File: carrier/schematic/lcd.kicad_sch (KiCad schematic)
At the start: 17 parts, among them J12001 AFC07-S40FCA-00, U12001 SY7201ABC

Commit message: board: four board-management HW blocks on a manually-gated +3V3_AUX (BOARDHW)
The four services the carrier was missing — all behind ONE manual power enable
(C1) on two new sheets split so neither defeats the placer's rail-stub router:

  board_aux       — the gate + I2C isolator (infrastructure)
  board_services  — ID-EEPROM + RTC + watchdog + QWIIC (the peripherals)

WHAT LANDED
  * 24AA025E48 (C129895)  ID-EEPROM with a factory EUI-48 **MAC** for the
      LAN8720/RJ45 — strapped 0x51 (0x50 is the FMC EEPROM).
  * RV-3028-C7 (C3019759) I2C RTC, integrated DTCXO (no crystal), CR1220 coin
      cell (KH-CR1220-2) with auto-switchover, 0x52.
  * TPS3823-33 (C7719)    supervisor + windowed watchdog.
  * ZX-SH1.0-4PWT (C7430446)  QWIIC / STEMMA-QT expansion (gated 3V3 + the
      isolated AUX I2C).
  * SY6280 gate + DSHP04 DIP + PCA9306 isolator complete the infrastructure.

CONSTRAINTS (the user's three standing requirements)
  C1 manual enable "like the previous": +3V3_AUX is a SY6280 load switch whose
     EN is a default-OFF DSHP04 DIP (100k pulldown) — the same gated-module
     idiom, self-contained so it touches none of the dense rail/EN sheets.
  C2 "no watchdog reset during power-up": THREE independent guards — (1) the
     supervisor's VDD is the default-OFF +3V3_AUX, so it is UNPOWERED through
     power-up; (2) the TPS3823 disables its watchdog while WDI floats, and WDI
     is driven only by the PL (WATCHDOG_KICK, Hi-Z until the fabric is up); (3)
     RESET# is a firmware-mediated PL EVENT (J3.31), never a rail/POR line.
  C3 Zynq-agnostic: the only SoM-side signals (the 2 watchdog lines) ride PL
     bank-35 IO by their contract net names (IO_L16_N/P_35 -> J3.29/31); xdc.py
     emits the constraints live — nothing hard-codes the Zynq part.

LAW 0 (electrical integrity): the peripherals sit on the GATED rail but their
bus is the always-on STM32_I2C2 management bus. A PCA9306 bridges them with EN
tied to +3V3_AUX, so the switch OPENS whenever the rail is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
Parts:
- renumbered C12001 to C14001, C12002 to C14002, C12003 to C14003, D12001 to D14001, J12001 to J14001, L12001 to L14001, R12001 to R14001, R12002 to R14002, R12003 to R14003, R12004 to R14004, R12005 to R14005, R12006 to R14006, R12007 to R14007, TP12001 to TP14001, TP12002 to TP14002, TP12003 to TP14003, U12001 to U14001

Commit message: audit fixes: QWIIC ESD on its own sheet + firmware I2C-map completeness
Acting on a multi-agent adversarial re-audit of the 28-sheet board. Each
finding was independently re-verified before action — two confident "HIGH"
findings were FALSE POSITIVES whose proposed fixes would have INTRODUCED bugs,
and are documented-rejected, not applied:

  * "DSHP04 switches in parallel" — wrong. The footprint pads prove the pairing
    by physical opposition (switch n = pads n & 9-n): switch 1 = pads 1&8 is the
    only one on EN_AUX; the other even pins (2/4/6) are NC, identical to the
    proven bringup_rails SW6 idiom. The proposed "fix" (pins 1+2) wires two
    DIFFERENT switches and would leave EN_AUX permanently pulled down — the rail
    could never enable.
  * "PCA9306 EN floats when AUX is off" — wrong. A 100k to a 0 V rail pulls EN
    to 0 V (disabled), which is exactly TI's recommended "isolate when the gated
    side is unpowered" connection. No float.

REAL findings actioned:

1. QWIIC connector lacked ESD (every other external connector has it). Moved the
   QWIIC out of board_services onto its own sheet board_qwiic (the carrier's
   connectors-get-their-own-sheet idiom — rj45_connector, usb_uart_connector)
   and added a USBLC6-2SC6 low-cap ESD array at the connector (1<->6 / 3<->4
   passthrough, clamp ref +3V3_AUX). The dedicated sheet also keeps both sheets
   sparse enough for the rail-stub router. board_services drops to 9 parts.

2. schgen/firmware.py loaded only 7 sheets, so the SC-firmware contract + its
   I2C address-collision check were BLIND to the new devices. Added board_aux/
   board_services to SOURCES and three address rows: FMC-EEPROM 0x50, ID-EEPROM
   0x51 (DERIVED from the 24AA025E48 A1/A0 straps, so a mis-strap to 0x50 now
   trips the collision check against the FMC EEPROM), RTC 0x52. The firmware can
   now address the EUI-48 MAC EEPROM and the RTC. 114 -> 117 #defines.

3. board_services docstring clarified (EEPROM/RTC are on the PCA9306-i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
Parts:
- renumbered C14001 to C15001, C14002 to C15002, C14003 to C15003, D14001 to D15001, J14001 to J15001, L14001 to L15001, R14001 to R15001, R14002 to R15002, R14003 to R15003, R14004 to R15004, R14005 to R15005, R14006 to R15006, R14007 to R15007, TP14001 to TP15001, TP14002 to TP15002, TP14003 to TP15003, U14001 to U15001

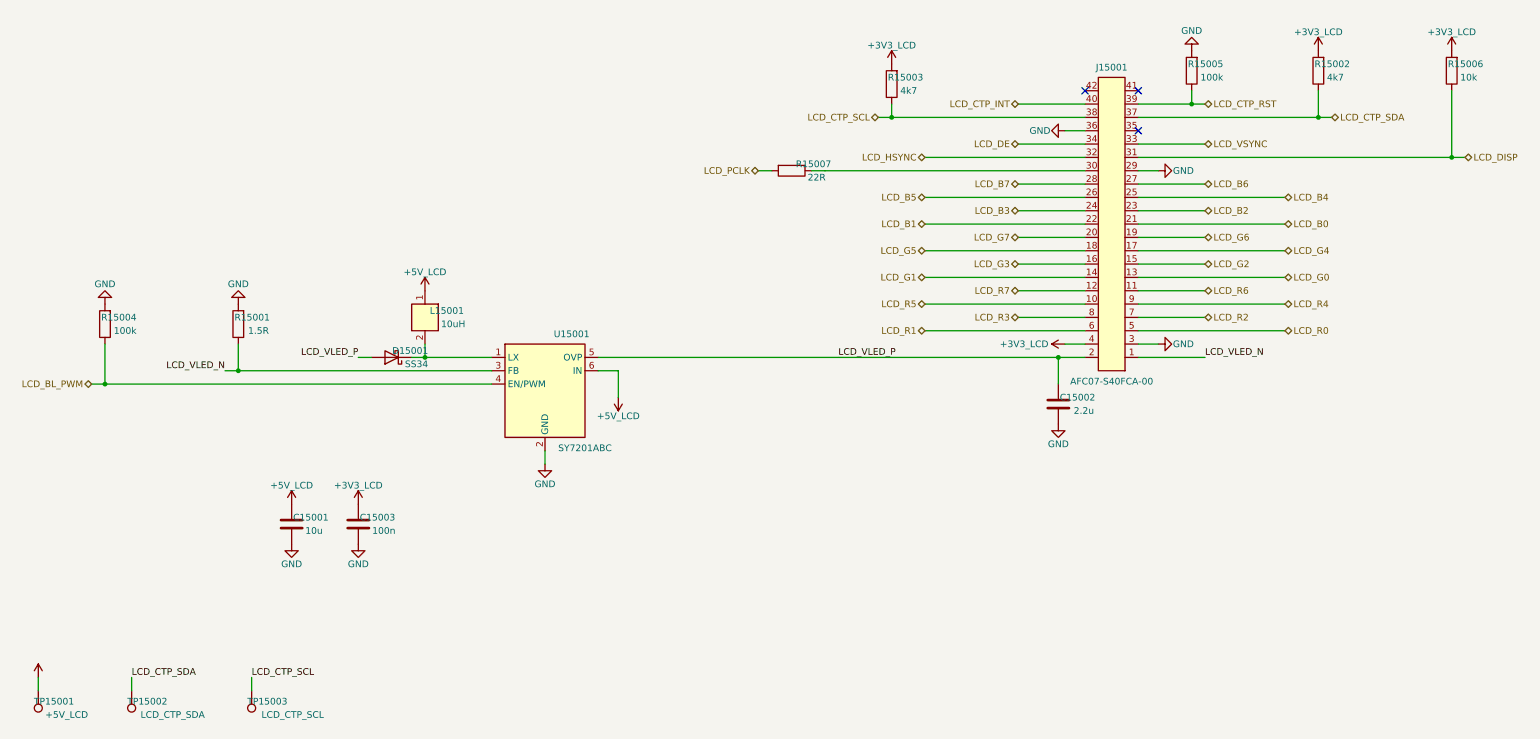
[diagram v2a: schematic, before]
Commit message: hdmi_tx + lcd: add the dossier-mandated 10u bulk on the gated rails (audit-4)
Completeness audit (what's MISSING). Two gated module rails carried only their
100n decap, while their dossiers explicitly mandate bulk AND every peer module
(camera/pmod/microsd 10-22u) has it — a real gap the per-pin design_rules gate
can't see (it audits IC supply pins, not consumed POWER rails):
  * +3V3_HDMI_TX (hdmi_tx.py) — bringup_power_gating.md 3.2 "each module owns
    its bulk". Added 10u 0805 (C15850).
  * +3V3_LCD (lcd.py) — lcd_backlight.md 3.1 "10uF + 100n" on panel VDD; only
    the 100n was present. Added 10u 0805.

Rejected/deferred from the same audit (re-verified): the +3V3_HDMI_RX bulk (one
~1mA load — design choice), +5V_HDMI_TX (already decoupled at the switch), and
+3V3_AUX bulk (board_aux output cap present). Two ESD findings are documented as
REVIEW items, NOT auto-applied: LCD-FFC ESD (the dossier consciously defers it +
the sheet is dense) and FMC ESD (FMC is a board-to-board mezzanine — ESD on LVDS
degrades SI and is non-standard).

board PASS @ 29 sheets, all gates green, 29 goldens blessed, selftest 53/53 +
hash-seed, m1, pytest 181.

Co-Authored-By: Claude Opus 4.8 <noreply@anthropic.com>
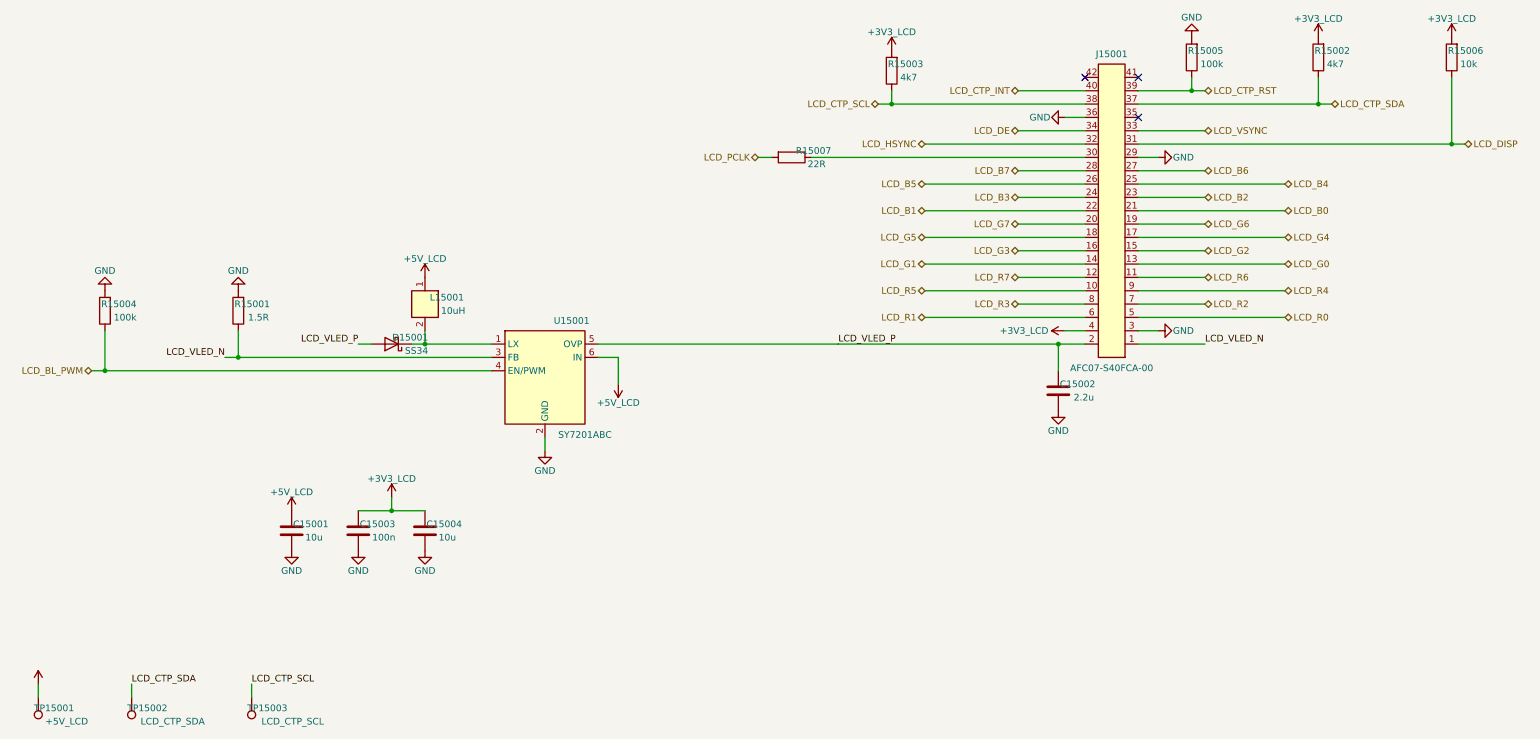
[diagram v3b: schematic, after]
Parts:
- added TP15003: LCD_CTP_SCL, TestPoint:TestPoint_Pad_D1.5mm, symbol Connector:TestPoint
- C15004: renamed from TP15001; value +5V_LCD -> 10u; footprint TestPoint:TestPoint_Pad_D1.5mm -> Capacitor_SMD:C_0805_2012Metric; symbol Connector:TestPoint -> Device:C; BOM exclude -> (none); LCSC (none) -> C15850
- TP15001: renamed from TP15002; value LCD_CTP_SDA -> +5V_LCD
- TP15002: renamed from TP15003; value LCD_CTP_SCL -> LCD_CTP_SDA
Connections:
- net +3V3_LCD: now also C15004.1
- net +5V_LCD: now also TP15001.1; no longer C15004.1
- net GND: now also C15004.2
- net LCD_CTP_SCL: now also TP15003.1; no longer TP15002.1
- net LCD_CTP_SDA: now also TP15002.1; no longer TP15001.1
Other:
- moved on the sheet: C15001, C15002, C15003, D15001, J15001, L15001, R15001, R15002, R15003, R15004, R15005, R15006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

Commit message: lcd: ESD-clamp the user-touchable touch-I2C at the FFC (your call, review #5)
The 40-pin LCD FFC is user-touchable; the dossier had deferred ESD. Per your
decision, the touch-I2C pair (CTP_SDA/SCL) is now clamped at the connector by a
USBLC6-2SC6 (the board's standard low-cap ESD array; 1<->6 / 3<->4 passthrough):
the external FFC pins on U2.1/U2.3, the protected pair (-> the pull-ups + PL) on
U2.6/U2.4, clamp ref the ALWAYS-ON +3V3 (= bank-13 VCCO) so protection holds
even with the gated +3V3_LCD panel rail off. The dense LCD sheet still routes
clean. board PASS @ 29 sheets, all gates green, 29 goldens blessed, selftest
53/53 + hash-seed, m1, pytest 181.

Co-Authored-By: Claude Opus 4.8 <noreply@anthropic.com>
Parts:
- added TP15003: LCD_CTP_SCL, TestPoint:TestPoint_Pad_D1.5mm, symbol Connector:TestPoint
- C15001: renamed from C15003; value 100n -> 10u; footprint Capacitor_SMD:C_0603_1608Metric -> Capacitor_SMD:C_0805_2012Metric; LCSC C1591 -> C15850
- C15002: renamed from C15001; value 10u -> 2.2u; LCSC C15850 -> C125847
- C15003: renamed from C15004; value 10u -> 100n; footprint Capacitor_SMD:C_0805_2012Metric -> Capacitor_SMD:C_0603_1608Metric; LCSC C15850 -> C1591
- C15004: renamed from TP15001; value +5V_LCD -> 10u; footprint TestPoint:TestPoint_Pad_D1.5mm -> Capacitor_SMD:C_0805_2012Metric; symbol Connector:TestPoint -> Device:C; BOM exclude -> (none); LCSC (none) -> C15850
- D15001: renamed from C15002; value 2.2u -> SS34; footprint Capacitor_SMD:C_0805_2012Metric -> Diode_SMD:D_SMA; symbol Device:C -> Device:D_Schottky; LCSC C125847 -> C8678
- J15001: renamed from R15001; value 1.5R -> AFC07-S40FCA-00; footprint Resistor_SMD:R_0603_1608Metric -> AFC07-S40FCA-00:AFC07-S40FCA-00; symbol Device:R -> AFC07-S40FCA-00:AFC07-S40FCA-00; LCSC C22769 -> C262572
- L15001: renamed from R15006; value 10k -> 10uH; footprint Resistor_SMD:R_0603_1608Metric -> SWPA4030S100MT:SWPA4030S100MT; symbol Device:R -> SWPA4030S100MT:SWPA4030S100MT; LCSC C25804 -> C38117
- R15001: renamed from R15004; value 100k -> 1.5R; LCSC C25803 -> C22769
- R15002: renamed from L15001; value 10uH -> 4k7; footprint SWPA4030S100MT:SWPA4030S100MT -> Resistor_SMD:R_0603_1608Metric; symbol SWPA4030S100MT:SWPA4030S100MT -> Device:R; LCSC C38117 -> C23162
- R15003: renamed from D15001; value SS34 -> 4k7; footprint Diode_SMD:D_SMA -> Resistor_SMD:R_0603_1608Metric; symbol Device:D_Schottky -> Device:R; LCSC C8678 -> C23162
- R15004: renamed from R15002; value 4k7 -> 100k; LCSC C23162 -> C25803
- R15005: renamed from R15003; value 4k7 -> 100k; LCSC C23162 -> C25803
- R15006: renamed from J15001; value AFC07-S40FCA-00 -> 10k; footprint AFC07-S40FCA-00:AFC07-S40FCA-00 -> Resistor_SMD:R_0603_1608Metric; symbol AFC07-S40FCA-00:AFC07-S40FCA-00 -> Device:R; LCSC C262572 -> C25804
- TP15001: renamed from TP15002; value LCD_CTP_SDA -> +5V_LCD
- TP15002: renamed from TP15003; value LCD_CTP_SCL -> LCD_CTP_SDA
- U15001: renamed from R15005; value 100k -> SY7201ABC; footprint Resistor_SMD:R_0603_1608Metric -> SY7201ABC:SY7201ABC; symbol Device:R -> SY7201ABC:SY7201ABC; LCSC C25803 -> C82173
- U15002: renamed from U15001; value SY7201ABC -> USBLC6-2SC6; footprint SY7201ABC:SY7201ABC -> USBLC6-2SC6:USBLC6-2SC6; symbol SY7201ABC:SY7201ABC -> USBLC6-2SC6:USBLC6-2SC6; LCSC C82173 -> C7519
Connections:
- net +3V3_LCD: now also C15004.1, J15001.4, R15002.2, R15003.2, R15006.2; no longer C15001.1, L15001.2, R15004.2, R15005.2, R15006.4
- net +5V_LCD: now also C15001.1, L15001.1, TP15001.1, U15001.6 (IN); no longer C15002.1, C15004.1, R15002.1, U15002.6 (IN)
- net GND: now also C15004.2, J15001.29, J15001.3, J15001.36, R15004.2, R15005.2; no longer D15001.2, J15001.2, R15006.29, R15006.3, R15006.36
- net LCD_B0: now also J15001.21; no longer R15006.21
- net LCD_B1: now also J15001.22; no longer R15006.22
- net LCD_B2: now also J15001.23; no longer R15006.23
- net LCD_B3: now also J15001.24; no longer R15006.24
- net LCD_B4: now also J15001.25; no longer R15006.25
- net LCD_B5: now also J15001.26; no longer R15006.26
- net LCD_B6: now also J15001.27; no longer R15006.27
- net LCD_B7: now also J15001.28; no longer R15006.28
- net LCD_BL_PWM: now also R15004.1, U15001.4 (EN/PWM); no longer R15001.1, U15002.4 (EN/PWM)
- net LCD_CTP_INT: now also J15001.40; no longer R15006.40
- net LCD_CTP_RST: now also J15001.39, R15005.1; no longer R15006.39, U15001.1
- net LCD_CTP_SCL: now also R15003.1, U15002.4, TP15003.1; no longer R15005.1, R15006.38, TP15002.1
- net LCD_CTP_SDA: now also R15002.1, TP15002.1, U15002.6; no longer R15004.1, R15006.37, TP15001.1
- net LCD_DE: now also J15001.34; no longer R15006.34
- net LCD_DISP: now also J15001.31, R15006.1; no longer L15001.1, R15006.31
- net LCD_G0: now also J15001.13; no longer R15006.13
- net LCD_G1: now also J15001.14; no longer R15006.14
- net LCD_G2: now also J15001.15; no longer R15006.15
- net LCD_G3: now also J15001.16; no longer R15006.16
- net LCD_G4: now also J15001.17; no longer R15006.17
- net LCD_G5: now also J15001.18; no longer R15006.18
- net LCD_G6: now also J15001.19; no longer R15006.19
- net LCD_G7: now also J15001.20; no longer R15006.20
- net LCD_HSYNC: now also J15001.32; no longer R15006.32
- net LCD_R0: now also J15001.5; no longer R15006.5
- net LCD_R1: now also J15001.6; no longer R15006.6
- net LCD_R2: now also J15001.7; no longer R15006.7
- net LCD_R3: now also J15001.8; no longer R15006.8
- net LCD_R4: now also J15001.9; no longer R15006.9
- net LCD_R5: now also J15001.10; no longer R15006.10
- net LCD_R6: now also J15001.11; no longer R15006.11
- net LCD_R7: now also J15001.12; no longer R15006.12
- net LCD_VLED_N: now also R15001.1, U15001.3 (FB); no longer R15006.1, U15002.3 (FB)
- net LCD_VLED_P: now also C15002.1, D15001.2 (A), J15001.2, U15001.5 (OVP); no longer D15001.1, R15003.2 (A), R15006.2, U15002.5 (OVP)
- net LCD_VSYNC: now also J15001.33; no longer R15006.33
- net at R15007.1: now also J15001.30; no longer R15006.30
- new net: D15001.1 (K), L15001.2, U15001.1 (LX)
- new net +3V3: U15002.5
- new net CTP_SCL_FFC: J15001.38, U15002.3
- new net CTP_SDA_FFC: J15001.37, U15002.1
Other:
- moved on the sheet: C15001, C15002, C15003, R15001, R15004, R15005, R15007, TP15001, TP15002

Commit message: bom: sourcing risk+cost report + C1591->C14663 (Extended->Basic 100n)
Stream F — live JLCPCB/LCSC sourcing pass over all 95 distinct BOM parts.

Report: carrier/manufacturing/SOURCING.md — per-part stock / Basic-vs-Extended
/ unit price / risk + flagged second sources, and a rollup (94 parts post-swap,
64 Extended of which 2 Preferred -> 62 feeder fees = ~$186, 15 parts <5k stock,
6 procurement-critical <300). Data from the JLCPCB parts API (live).

Applied swap (only clean Basic drop-in on the board): 100 nF 0603 decoupling
C1591 (Samsung CL10B104KB8NNNC, Extended, 2.08M) -> C14663 (YAGEO
CC0603KRX7R9BB104, Basic, 17.8M). IDENTICAL 100nF/50V/X7R/+-10%/0603, same
footprint+symbol -> netlist & render byte-identical; ratings.py already carries
C14663 with matching ratings. Merges 71 Extended + 12 existing-Basic positions
onto one 83-piece Basic line: removes one Extended feeder fee, cheaper unit,
8.5x more stock.

Everything else is REPORT-ONLY: every other Extended part is
Extended-by-necessity (no JLC-Basic equivalent — precise E96 values, specialty
ICs/connectors) or has only a footprint-mismatched / MPN-ambiguous alternate.
Also flagged (not fixed): C25750 ("40.2k" power:R1) currently resolves on LCSC
to a 120k 0402 part — a data-integrity bug; recommend C12447 after intent check.

Gates: part-rules PASS (132 checks, 0 findings); board PASS (33 sheets, golden
renders 33/33 match, DRC 0); selftest 59/59; m1_rc PASS; pytest 219 passed.
BOM regen deterministic (md5 stable).

Co-Authored-By: Claude Opus 4.8 <noreply@anthropic.com>
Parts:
- C15003: LCSC C1591 -> C14663
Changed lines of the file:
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@@
 		(property
 			"LCSC"
-			"C1591"
+			"C14663"
 			(at 62.23 176.53 0)
 			(effects

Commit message: fix: 3 CRITICAL electrical defects from the multi-agent audit (SW2 / LCD D1 / JTAG TDI-TDO)
A 69-agent electrical audit (35 per-subsystem + 7 cross-cutting, every finding
adversarially refuted) surfaced 3 board-dead CRITICAL defects that passed DRC/ERC/
netlist-equivalence. Each independently re-verified from the source artifacts before
fixing (per the "audits over-confirm; fixes can introduce bugs" rule):

1. SW2 (DSHP08) module DIP shorted all enables. Each DIP rocker bridges the two
   pads in the SAME COLUMN; the DSHP08 footprint numbers its bottom row 9..16
   (UNLIKE DSHP04's 8..5), so positions pair (n, n+8) — but the adapter re-used
   DSHP04's (n,17-n) diagonal, shorting +3V3_SC to itself on 1/3/5/7 and tying two
   enable nets on 2/4/6/8. All 7 module enables stuck off. FIX in the ADAPTER
   (+3V3_SC on top pins 1-8, BU_DIP nets on bottom pins 9-16) — NOT by renumbering
   the faithful EasyEDA footprint as the audit suggested (that would corrupt the
   real-part mapping; "never redraw parts"). DSHP08 is used only by SW2.
   + footprint-aware regression test (reads same-column pairs, asserts each rocker
     bridges +3V3_SC -> one unique BU_DIP enable) for SW2 and SW1.

2. LCD SY7201 boost catch diode D1 (SS34) reversed — cathode on LX, anode on the
   output, so the boost could never pump VLED+ (dead backlight). Device:D_Schottky
   is pin1=K/pin2=A; put K (D1.1) on the output, A (D1.2) on LX. The dossier was
   already correct; the netlist contradicted it.

3. usb_jtag CH347T TDI/TDO swapped — pin7=RTS0/MISO/TDO (bridge input), pin8=
   TXD0/MOSI/TDI (bridge output). DBG_FT_TDI sat on the input pin (buffer 2A had
   no driver) and DBG_FT_TDO on the output pin (collides with buffer 3Y when the
   bridge enables). Swapped to U1.8/U1.7; doc table corrected.

Verified: 148x137, DRC 0, netlist-equivalence PASS on all 35 sheets, every LAW gate
green, 68 subsystem tests pass.

Co-Authored-By: Claude Opus 4.8 <noreply@anthropic.com>
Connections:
- net LCD_VLED_P: now also D15001.1 (K); no longer D15001.2 (A)
- net at L15001.2, U15001.1 (LX): now also D15001.2 (A); no longer D15001.1 (K)
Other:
- moved on the sheet: D15001
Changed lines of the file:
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@@
 	(symbol
 		(lib_id "Device:D_Schottky")
-		(at 384.81 107.95 0)
+		(at 384.81 107.95 180)
 		(unit 1)
 		(exclude_from_sim no)
@@
 			"Reference"
 			"D15001"
-			(at 381.278 106.68 0)
+			(at 381.913 106.68 0)
 			(effects
 				(font
@@
 			"Value"
 			"SS34"
-			(at 380.072 109.22 0)
+			(at 380.707 109.22 0)
 			(effects
 				(font
